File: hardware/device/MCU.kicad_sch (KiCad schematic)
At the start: 28 parts, among them SW24 NRST, SW25 BOOT0, U1 BMDU, U18 STM32H743ZIT6

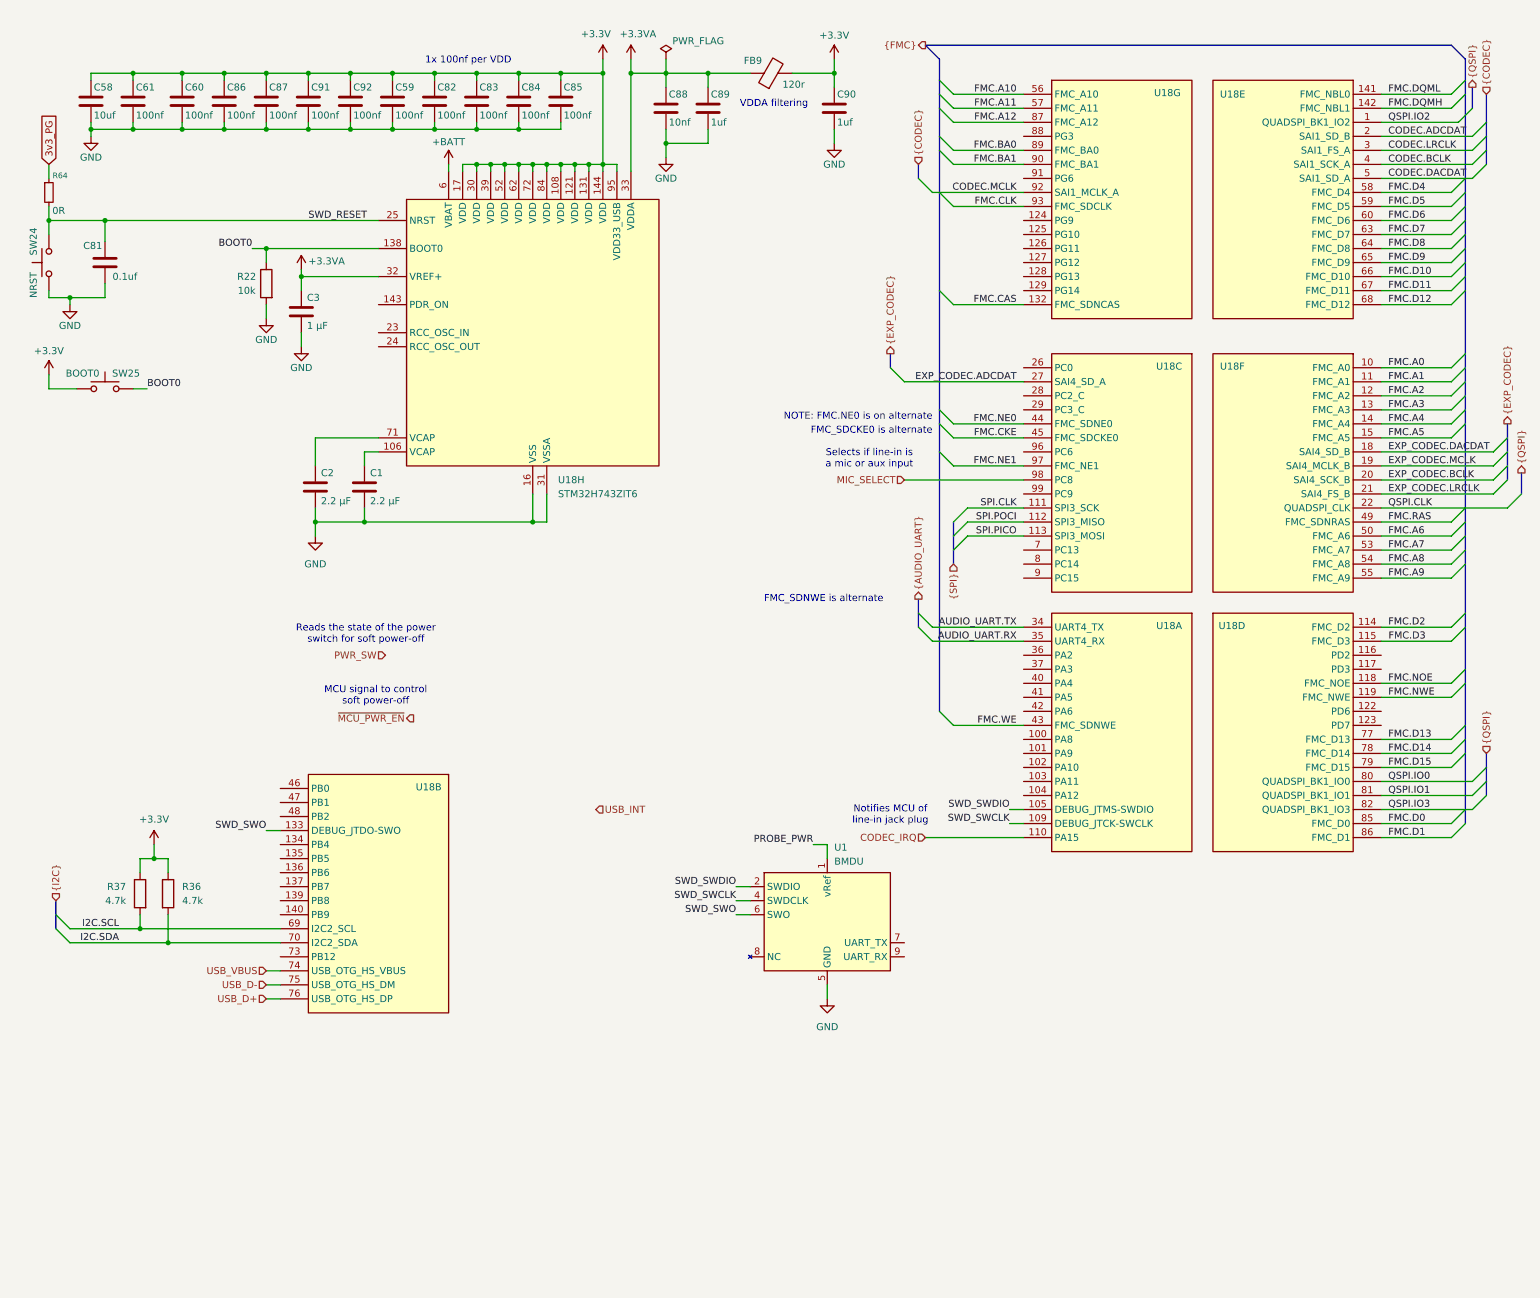
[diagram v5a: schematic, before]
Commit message: feat: various routing, footprint and schematic cleanup
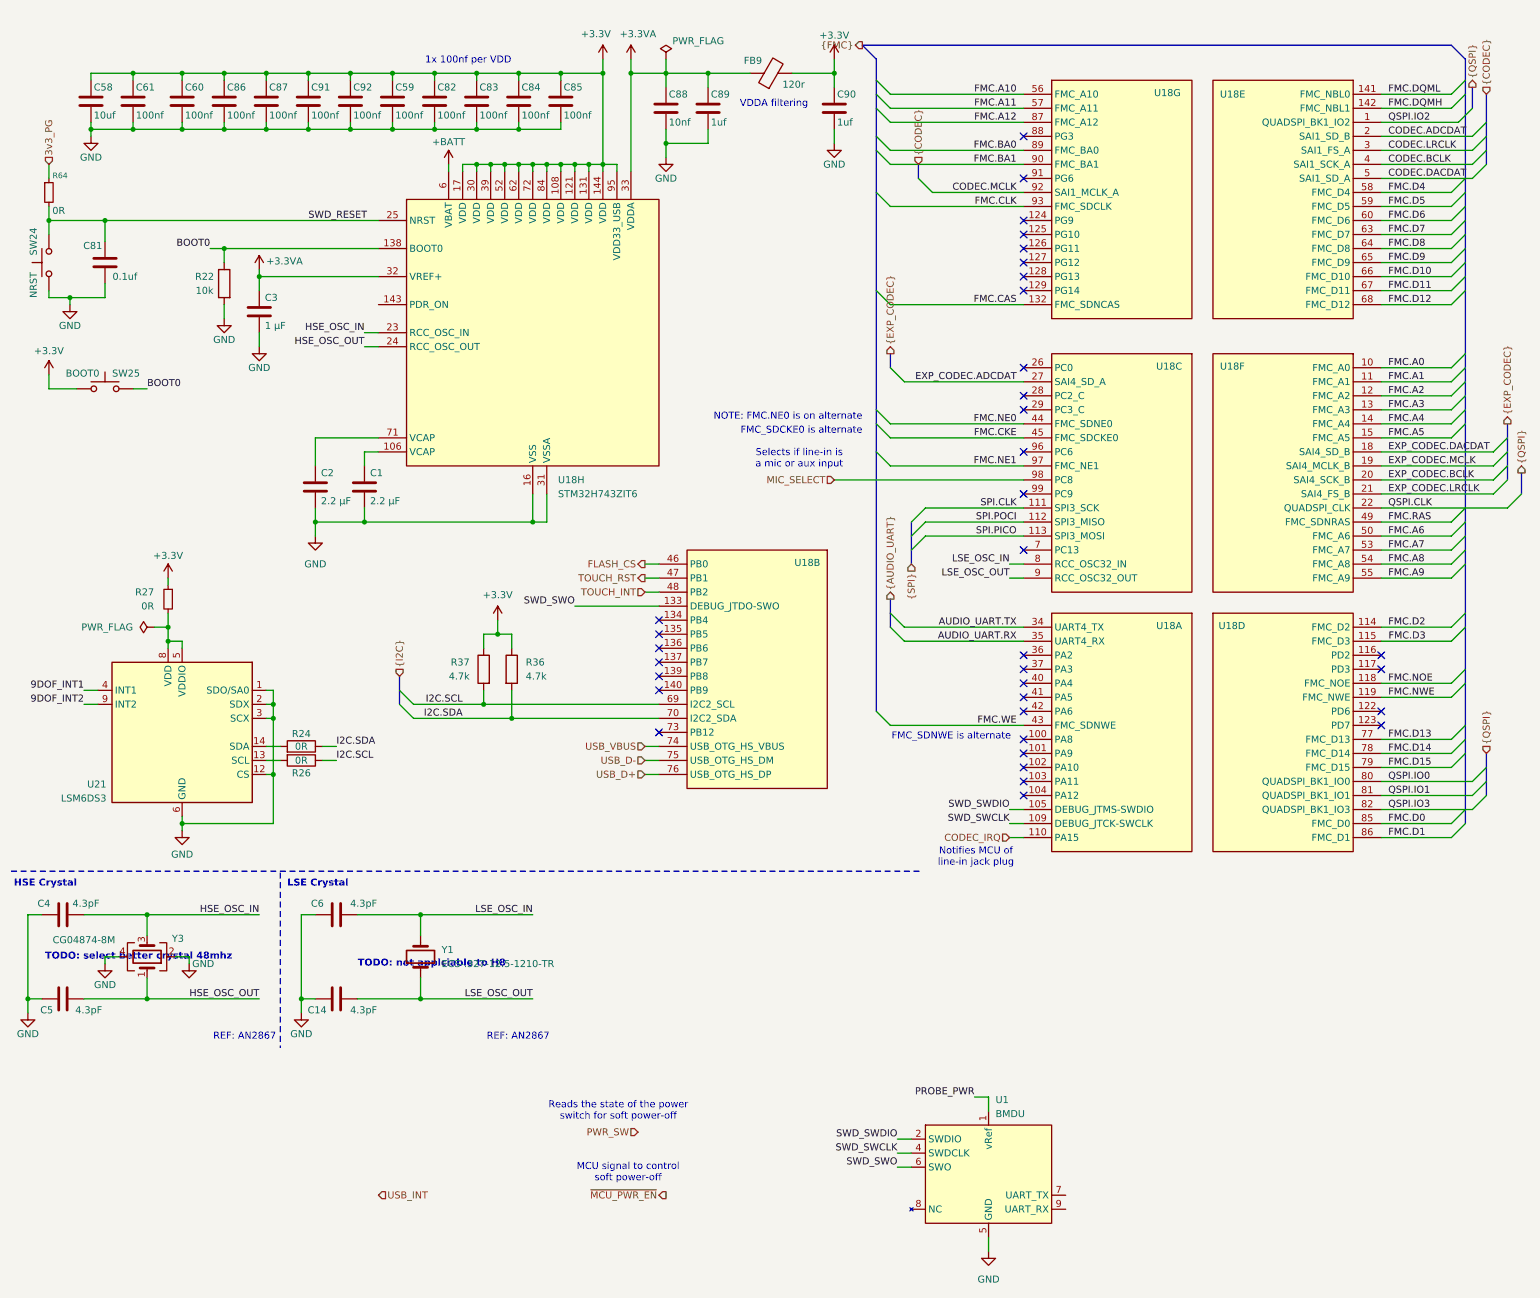
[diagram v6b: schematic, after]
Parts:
- added C14, C4, C5, C6: 4.3pF, Capacitor_SMD:C_0402_1005Metric, symbol Device:C
- added R24, R26: 0R, Resistor_SMD:R_0402_1005Metric, symbol Device:R
- added R27: 0R, Resistor_SMD:R_0402_1005Metric, symbol Device:R_Small
- added U21: LSM6DS3, Package_LGA:LGA-14_3x2.5mm_P0.5mm_LayoutBorder3x4y, symbol Sensor_Motion:LSM6DS3
- added Y1: ECS-.327-12.5-1210-TR, pocket_synth:XTAL_ECS-.327-12.5-1210-TR, symbol Device:Crystal
- added Y3: CG04874-8M, Crystal:Crystal_SMD_Abracon_ABM3B-4Pin_5.0x3.2mm, symbol Device:Crystal_GND24
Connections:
- net FMC.BA1 is gone; now on net {CODEC}: U18.90 (PG5)
- net +3.3V: now also R27.1
- net GND: now also C14.1, C4.1, C5.1, C6.1, U21.1 (SDO/SA0), U21.12 (CS), U21.2 (SDX), U21.3 (SCX), U21.6 (GND), U21.7 (GND), Y3.2, Y3.4
- net I2C.SCL: now also R26.1
- net I2C.SDA: now also R24.1
- net HSE_OSC_IN: now reaches U18.23 (PH0)
- net HSE_OSC_IN: now also C4.2, Y3.3
- net HSE_OSC_OUT: now reaches U18.24 (PH1)
- net HSE_OSC_OUT: now also C5.2, Y3.1
- net LSE_OSC_IN: now reaches U18.8 (PC14)
- net LSE_OSC_IN: now also C6.2, Y1.2
- net LSE_OSC_OUT: now reaches U18.9 (PC15)
- net LSE_OSC_OUT: now also C14.2, Y1.1
- net FLASH_CS: now reaches U18.46 (PB0)
- net TOUCH_RST: now reaches U18.47 (PB1)
- net TOUCH_INT: now reaches U18.48 (PB2)
- new net: R26.2, U21.13 (SCL)
- new net: R24.2, U21.14 (SDA)
- new net: R27.2, U21.5 (VDDIO), U21.8 (VDD)
- new net 9DOF_INT1: U21.4 (INT1)
- new net 9DOF_INT2: U21.9 (INT2)
- no-connect marks 0 -> 35
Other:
- note added: "HSE Crystal"
- note added: "LSE Crystal"
- note added: "REF: AN2867"
- note added: "TODO: not applciable to H8"
- note added: "TODO: select better crystal 48mhz"
- moved on the sheet: C3, R22, R36, R37, U1, U18B

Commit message: feat: fix incorrect HSE crystal
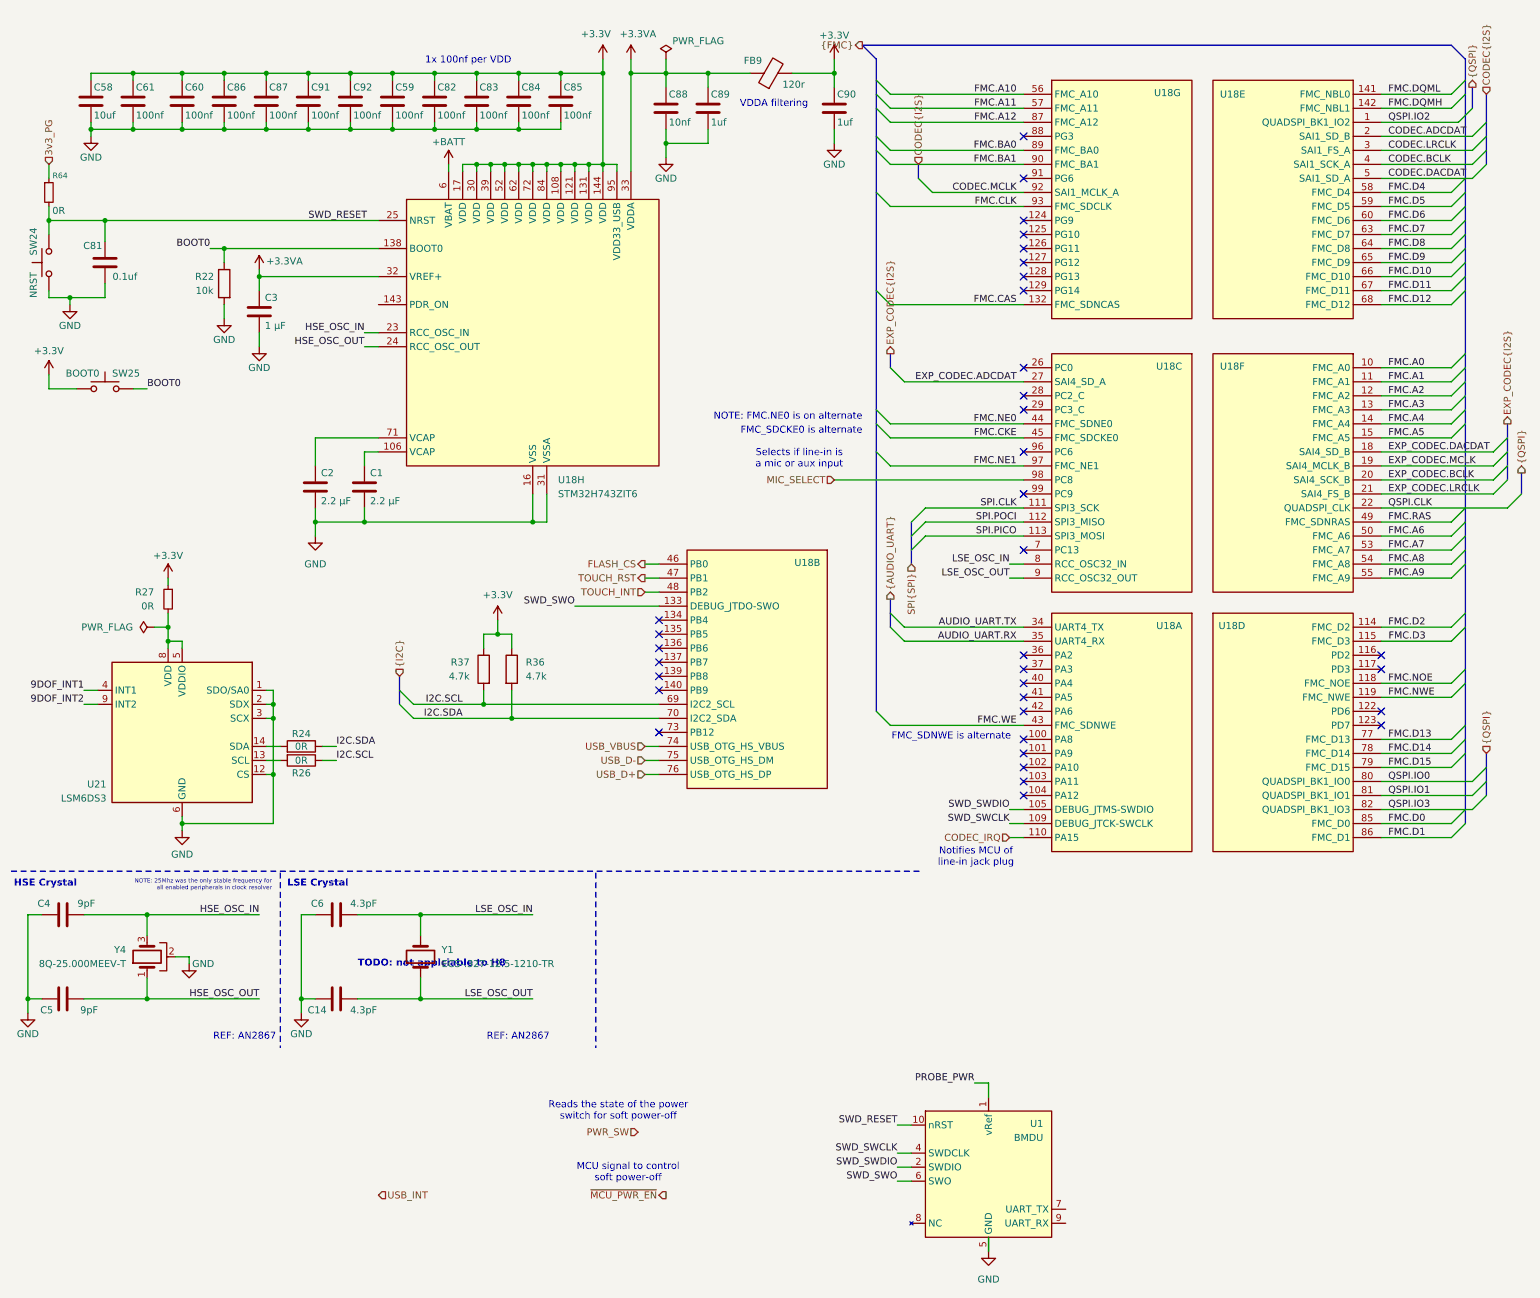
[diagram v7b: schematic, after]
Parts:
- removed Y3: CG04874-8M, Crystal:Crystal_SMD_Abracon_ABM3B-4Pin_5.0x3.2mm, symbol Device:Crystal_GND24
- added Y4: 8Q-25.000MEEV-T, pocket_synth:XTAL_8Q-25.000MEEV-T, symbol Device:Crystal_GND2
- C4, C5: value 4.3pF -> 9pF
- FB9: footprint (none) -> Inductor_SMD:L_0603_1608Metric
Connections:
- net GND: now also Y4.2
- net HSE_OSC_IN: now also Y4.3
- net HSE_OSC_OUT: now also Y4.1
- net SWD_RESET: now also U1.10 (nRST)
- net {CODEC} renamed CODEC{I2S}
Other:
- note added: "NOTE: 25Mhz was the only stable frequency for all enabled peripherals in clock resolver"
- note removed: "TODO: select better crystal 48mhz"

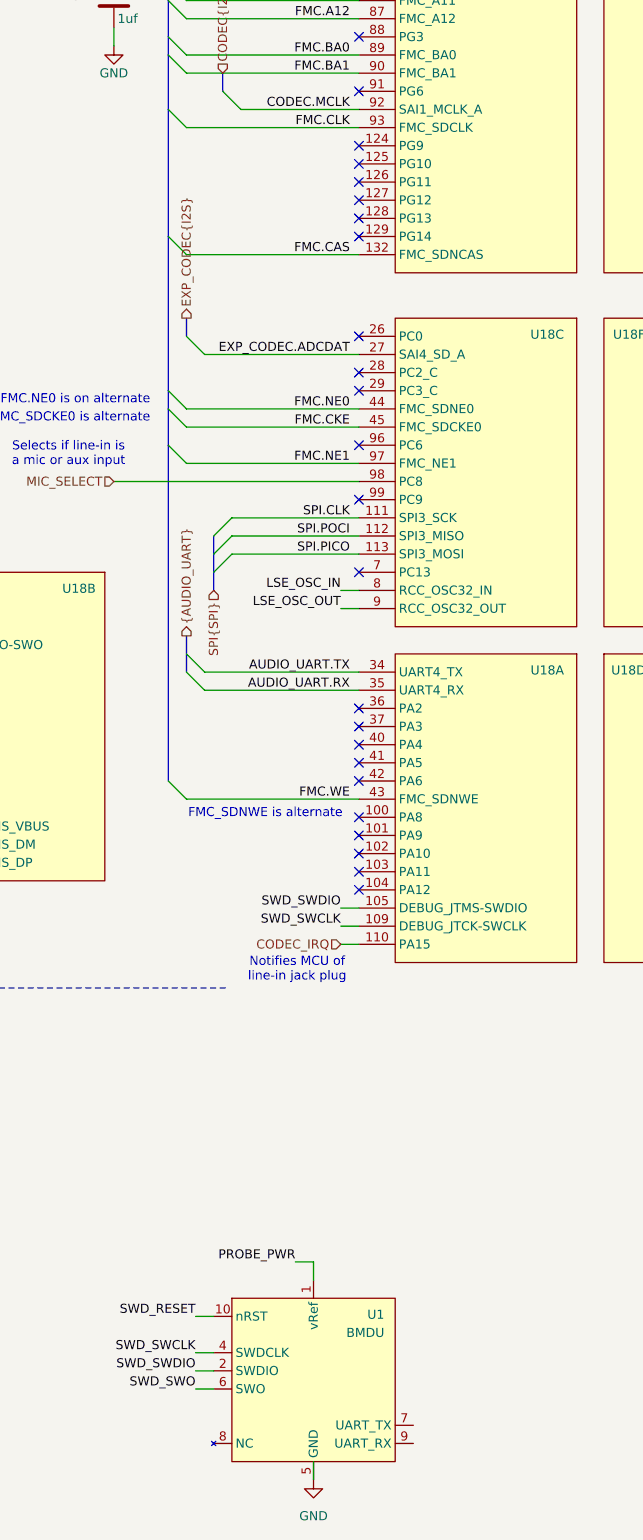
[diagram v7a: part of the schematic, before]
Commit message: feat: add SWD connector, route bluetooth, route velocity matrix
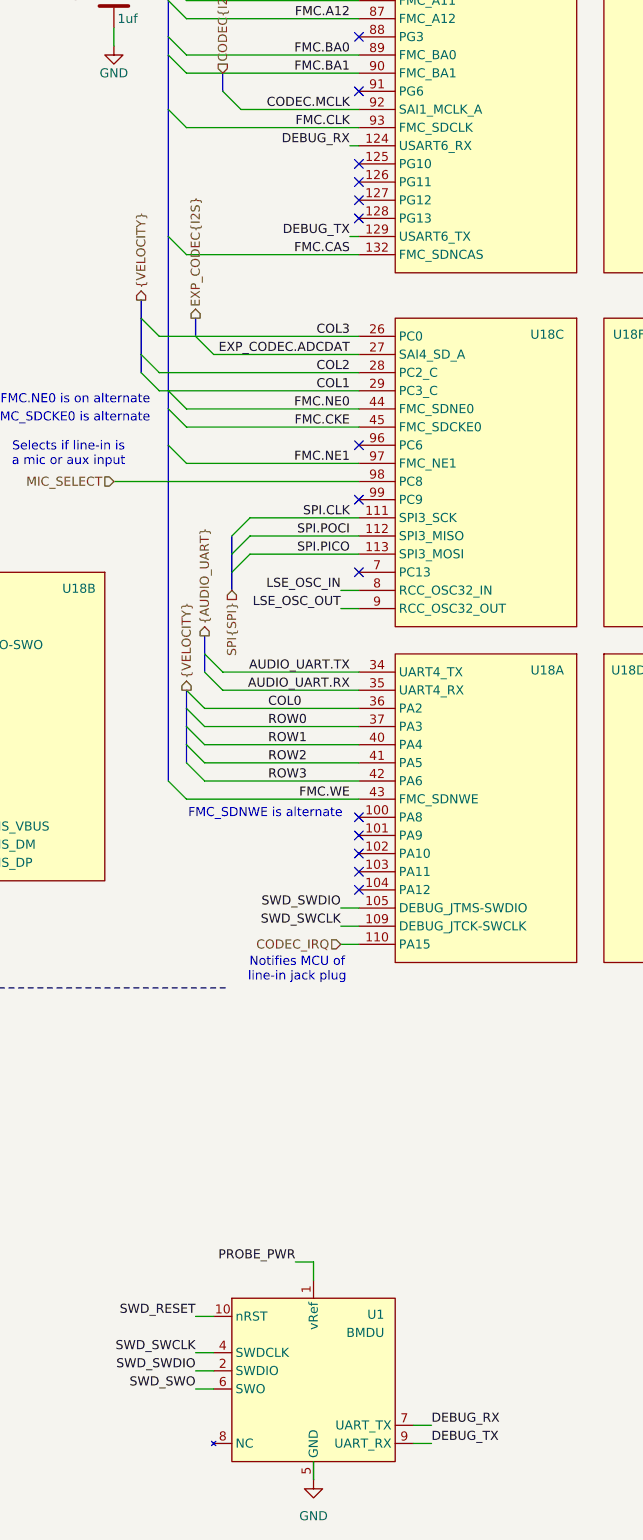
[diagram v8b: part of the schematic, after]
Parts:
- U1: footprint Connector_PinHeader_1.27mm:PinHeader_2x05_P1.27mm_Vertical -> pocket_synth:SAMTEC_FTSH-105-01-F-D-K
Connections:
- net COL0: now reaches U18.36 (PA2)
- net ROW0: now reaches U18.37 (PA3)
- net ROW1: now reaches U18.40 (PA4)
- net ROW2: now reaches U18.41 (PA5)
- net ROW3: now reaches U18.42 (PA6)
- net COL3: now reaches U18.26 (PC0)
- net COL2: now reaches U18.28 (PC2_C)
- net COL1: now reaches U18.29 (PC3_C)
- net DEBUG_RX: now reaches U18.124 (PG9)
- net DEBUG_RX: now also U1.7 (UART_TX)
- net DEBUG_TX: now reaches U18.129 (PG14)
- net DEBUG_TX: now also U1.9 (UART_RX)
- no-connect marks 35 -> 25
